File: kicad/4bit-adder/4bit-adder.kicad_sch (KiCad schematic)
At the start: 94 parts, among them J1 Screw_Terminal_01x02, K1 SR11-5V-200-2C-PH, K10 SR11-5V-200-2C-PH, K11 SR11-5V-200-2C-PH, K12 SR11-5V-200-2C-PH, K13 SR11-5V-200-2C-PH, K14 SR11-5V-200-2C-PH, K15 SR11-5V-200-2C-PH, K16 SR11-5V-200-2C-PH, K17 SR11-5V-200-2C-PH, K18 SR11-5V-200-2C-PH, K19 SR11-5V-200-2C-PH, K2 SR11-5V-200-2C-PH, K20 SR11-5V-200-2C-PH, K21 SR11-5V-200-2C-PH, K22 SR11-5V-200-2C-PH, K23 SR11-5V-200-2C-PH, K24 SR11-5V-200-2C-PH, K3 SR11-5V-200-2C-PH, K4 SR11-5V-200-2C-PH, K5 SR11-5V-200-2C-PH, K6 SR11-5V-200-2C-PH, K7 SR11-5V-200-2C-PH, K8 SR11-5V-200-2C-PH, K9 SR11-5V-200-2C-PH, SW1 SW_Wuerth_450301014042, SW3 A, SW4 B

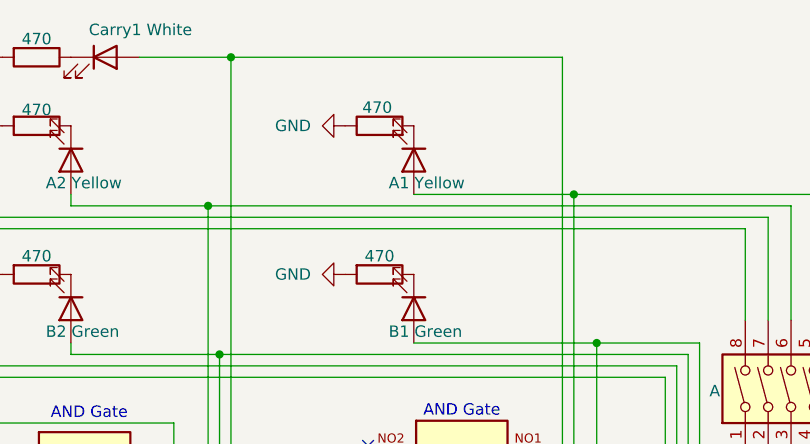
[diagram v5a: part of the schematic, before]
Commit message: wired top pad-A
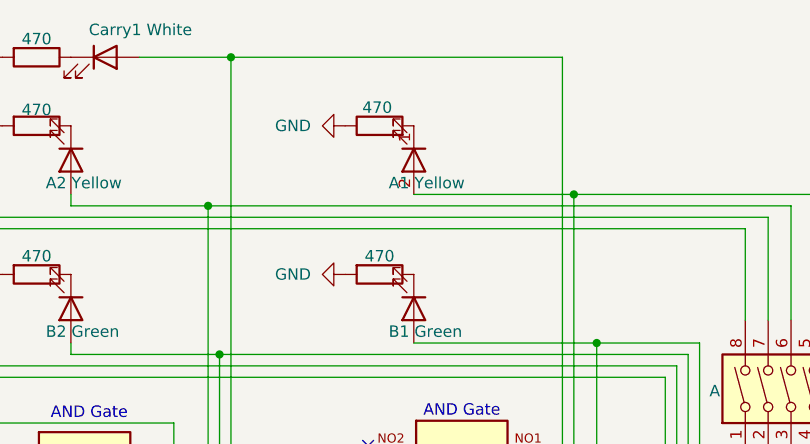
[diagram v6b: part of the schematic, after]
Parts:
- D1, D22, D23, D24, D26, D27, D28, D29, D3, D30, D31, D32, D33, D34, D35, D36, D37, D38, D39, D4, D40, D41, D42, D43, D44, D45, D46, D47, D48, D49, D5, D6, D7: footprint Diode_THT:D_DO-41_SOD81_P10.16mm_Horizontal -> Diode_SMD:D_SOD-123F
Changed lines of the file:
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@@
 			)
 		)
-		(property "Footprint" "Diode_THT:D_DO-41_SOD81_P10.16mm_Horizontal"
+		(property "Footprint" "Diode_SMD:D_SOD-123F"
 			(at 115.57 118.745 0)
 			(hide yes)
@@
 			)
 		)
-		(property "Footprint" "Diode_THT:D_DO-41_SOD81_P10.16mm_Horizontal"
+		(property "Footprint" "Diode_SMD:D_SOD-123F"
 			(at 115.57 95.885 0)
 			(hide yes)
@@
 			)
 		)
-		(property "Footprint" "Diode_THT:D_DO-41_SOD81_P10.16mm_Horizontal"
+		(property "Footprint" "Diode_SMD:D_SOD-123F"
 			(at 36.83 193.675 0)
 			(hide yes)
@@
 			)
 		)
-		(property "Footprint" "Diode_THT:D_DO-41_SOD81_P10.16mm_Horizontal"
+		(property "Footprint" "Diode_SMD:D_SOD-123F"
 			(at 35.56 95.885 0)
 			(hide yes)
@@
 			)
 		)
-		(property "Footprint" "Diode_THT:D_DO-41_SOD81_P10.16mm_Horizontal"
+		(property "Footprint" "Diode_SMD:D_SOD-123F"
 			(at 35.56 168.275 0)
 			(hide yes)
@@
 			)
 		)
-		(property "Footprint" "Diode_THT:D_DO-41_SOD81_P10.16mm_Horizontal"
+		(property "Footprint" "Diode_SMD:D_SOD-123F"
 			(at 99.06 85.725 0)
 			(hide yes)
@@
 			)
 		)
-		(property "Footprint" "Diode_THT:D_DO-41_SOD81_P10.16mm_Horizontal"
+		(property "Footprint" "Diode_SMD:D_SOD-123F"
 			(at 76.2 146.685 0)
 			(hide yes)
@@
 			)
 		)
-		(property "Footprint" "Diode_THT:D_DO-41_SOD81_P10.16mm_Horizontal"
+		(property "Footprint" "Diode_SMD:D_SOD-123F"
 			(at 76.2 118.745 0)
 			(hide yes)
@@
 			)
 		)
-		(property "Footprint" "Diode_THT:D_DO-41_SOD81_P10.16mm_Horizontal"
+		(property "Footprint" "Diode_SMD:D_SOD-123F"
 			(at 35.56 118.745 0)
 			(hide yes)
@@
 			)
 		)
-		(property "Footprint" "Diode_THT:D_DO-41_SOD81_P10.16mm_Horizontal"
+		(property "Footprint" "Diode_SMD:D_SOD-123F"
 			(at 157.48 95.885 0)
 			(hide yes)
@@
 			)
 		)
-		(property "Footprint" "Diode_THT:D_DO-41_SOD81_P10.16mm_Horizontal"
+		(property "Footprint" "Diode_SMD:D_SOD-123F"
 			(at 76.2 168.275 0)
 			(hide yes)
@@
 			)
 		)
-		(property "Footprint" "Diode_THT:D_DO-41_SOD81_P10.16mm_Horizontal"
+		(property "Footprint" "Diode_SMD:D_SOD-123F"
 			(at 76.2 193.675 0)
 			(hide yes)
@@
 			)
 		)
-		(property "Footprint" "Diode_THT:D_DO-41_SOD81_P10.16mm_Horizontal"
+		(property "Footprint" "Diode_SMD:D_SOD-123F"
 			(at 19.05 88.265 0)
 			(hide yes)
@@
 			)
 		)
-		(property "Footprint" "Diode_THT:D_DO-41_SOD81_P10.16mm_Horizontal"
+		(property "Footprint" "Diode_SMD:D_SOD-123F"
 			(at 115.57 146.685 0)
 			(hide yes)
@@
 			)
 		)
-		(property "Footprint" "Diode_THT:D_DO-41_SOD81_P10.16mm_Horizontal"
+		(property "Footprint" "Diode_SMD:D_SOD-123F"
 			(at 115.57 193.675 0)
 			(hide yes)
@@
 			)
 		)
-		(property "Footprint" "Diode_THT:D_DO-41_SOD81_P10.16mm_Horizontal"
+		(property "Footprint" "Diode_SMD:D_SOD-123F"
 			(at 115.57 73.025 0)
 			(hide yes)
@@
 			)
 		)
-		(property "Footprint" "Diode_THT:D_DO-41_SOD81_P10.16mm_Horizontal"
+		(property "Footprint" "Diode_SMD:D_SOD-123F"
 			(at 59.69 83.185 0)
 			(hide yes)
@@
 			)
 		)
-		(property "Footprint" "Diode_THT:D_DO-41_SOD81_P10.16mm_Horizontal"
+		(property "Footprint" "Diode_SMD:D_SOD-123F"
 			(at 19.05 83.185 0)
 			(hide yes)
@@
 			)
 		)
-		(property "Footprint" "Diode_THT:D_DO-41_SOD81_P10.16mm_Horizontal"
+		(property "Footprint" "Diode_SMD:D_SOD-123F"
 			(at 99.06 83.185 0)
 			(hide yes)
@@
 			)
 		)
-		(property "Footprint" "Diode_THT:D_DO-41_SOD81_P10.16mm_Horizontal"
+		(property "Footprint" "Diode_SMD:D_SOD-123F"
 			(at 76.2 215.265 0)
 			(hide yes)
@@
 			)
 		)
-		(property "Footprint" "Diode_THT:D_DO-41_SOD81_P10.16mm_Horizontal"
+		(property "Footprint" "Diode_SMD:D_SOD-123F"
 			(at 35.56 215.265 0)
 			(hide yes)
@@
 	)
 	(symbol
+		(lib_name "LED_1")
 		(lib_id "Device:LED")
 		(at 152.4 29.21 270)
@@
 			)
 		)
-		(property "Footprint" "Diode_THT:D_DO-41_SOD81_P10.16mm_Horizontal"
+		(property "Footprint" "Diode_SMD:D_SOD-123F"
 			(at 157.48 121.285 0)
 			(hide yes)
@@
 			)
 		)
-		(property "Footprint" "Diode_THT:D_DO-41_SOD81_P10.16mm_Horizontal"
+		(property "Footprint" "Diode_SMD:D_SOD-123F"
 			(at 35.56 73.025 0)
 			(hide yes)
@@
 			)
 		)
-		(property "Footprint" "Diode_THT:D_DO-41_SOD81_P10.16mm_Horizontal"
+		(property "Footprint" "Diode_SMD:D_SOD-123F"
 			(at 157.48 71.755 0)
 			(hide yes)
@@
 			)
 		)
-		(property "Footprint" "Diode_THT:D_DO-41_SOD81_P10.16mm_Horizontal"
+		(property "Footprint" "Diode_SMD:D_SOD-123F"
 			(at 35.56 146.685 0)
 			(hide yes)
@@
 			)
 		)
-		(property "Footprint" "Diode_THT:D_DO-41_SOD81_P10.16mm_Horizontal"
+		(property "Footprint" "Diode_SMD:D_SOD-123F"
 			(at 59.69 88.265 0)
 			(hide yes)
@@
 			)
 		)
-		(property "Footprint" "Diode_THT:D_DO-41_SOD81_P10.16mm_Horizontal"
+		(property "Footprint" "Diode_SMD:D_SOD-123F"
 			(at 77.47 95.885 0)
 			(hide yes)
@@
 			)
 		)
-		(property "Footprint" "Diode_THT:D_DO-41_SOD81_P10.16mm_Horizontal"
+		(property "Footprint" "Diode_SMD:D_SOD-123F"
 			(at 115.57 215.265 0)
 			(hide yes)
@@
 			)
 		)
-		(property "Footprint" "Diode_THT:D_DO-41_SOD81_P10.16mm_Horizontal"
+		(property "Footprint" "Diode_SMD:D_SOD-123F"
 			(at 19.05 85.725 0)
 			(hide yes)
@@
 			)
 		)
-		(property "Footprint" "Diode_THT:D_DO-41_SOD81_P10.16mm_Horizontal"
+		(property "Footprint" "Diode_SMD:D_SOD-123F"
 			(at 76.2 73.025 0)
 			(hide yes)
@@
 			)
 		)
-		(property "Footprint" "Diode_THT:D_DO-41_SOD81_P10.16mm_Horizontal"
+		(property "Footprint" "Diode_SMD:D_SOD-123F"
 			(at 99.06 88.265 0)
 			(hide yes)
@@
 			)
 		)
-		(property "Footprint" "Diode_THT:D_DO-41_SOD81_P10.16mm_Horizontal"
+		(property "Footprint" "Diode_SMD:D_SOD-123F"
 			(at 59.69 85.725 0)
 			(hide yes)
@@
 			)
 		)
-		(property "Footprint" "Diode_THT:D_DO-41_SOD81_P10.16mm_Horizontal"
+		(property "Footprint" "Diode_SMD:D_SOD-123F"
 			(at 115.57 168.275 0)
 			(hide yes)

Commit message: finished pcb wiring
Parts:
- D1, D22, D23, D24, D26, D27, D28, D29, D3, D30, D31, D32, D33, D34, D35, D36, D37, D38, D39, D4, D40, D41, D42, D43, D44, D45, D46, D47, D48, D49, D5, D6, D7: footprint Diode_SMD:D_SOD-123F -> Diode_THT:D_T-1_P5.08mm_Horizontal
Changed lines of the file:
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@@
 			)
 		)
-		(property "Footprint" "Diode_SMD:D_SOD-123F"
+		(property "Footprint" "Diode_THT:D_T-1_P5.08mm_Horizontal"
 			(at 115.57 118.745 0)
 			(hide yes)
@@
 	)
 	(symbol
+		(lib_name "1N4003_1")
 		(lib_id "Diode:1N4003")
 		(at 115.57 100.33 180)
@@
 			)
 		)
-		(property "Footprint" "Diode_SMD:D_SOD-123F"
+		(property "Footprint" "Diode_THT:D_T-1_P5.08mm_Horizontal"
 			(at 115.57 95.885 0)
 			(hide yes)
@@
 			)
 		)
-		(property "Footprint" "Diode_SMD:D_SOD-123F"
+		(property "Footprint" "Diode_THT:D_T-1_P5.08mm_Horizontal"
 			(at 36.83 193.675 0)
 			(hide yes)
@@
 			)
 		)
-		(property "Footprint" "Diode_SMD:D_SOD-123F"
+		(property "Footprint" "Diode_THT:D_T-1_P5.08mm_Horizontal"
 			(at 35.56 95.885 0)
 			(hide yes)
@@
 			)
 		)
-		(property "Footprint" "Diode_SMD:D_SOD-123F"
+		(property "Footprint" "Diode_THT:D_T-1_P5.08mm_Horizontal"
 			(at 35.56 168.275 0)
 			(hide yes)
@@
 			)
 		)
-		(property "Footprint" "Diode_SMD:D_SOD-123F"
+		(property "Footprint" "Diode_THT:D_T-1_P5.08mm_Horizontal"
 			(at 99.06 85.725 0)
 			(hide yes)
@@
 			)
 		)
-		(property "Footprint" "Diode_SMD:D_SOD-123F"
+		(property "Footprint" "Diode_THT:D_T-1_P5.08mm_Horizontal"
 			(at 76.2 146.685 0)
 			(hide yes)
@@
 			)
 		)
-		(property "Footprint" "Diode_SMD:D_SOD-123F"
+		(property "Footprint" "Diode_THT:D_T-1_P5.08mm_Horizontal"
 			(at 76.2 118.745 0)
 			(hide yes)
@@
 			)
 		)
-		(property "Footprint" "Diode_SMD:D_SOD-123F"
+		(property "Footprint" "Diode_THT:D_T-1_P5.08mm_Horizontal"
 			(at 35.56 118.745 0)
 			(hide yes)
@@
 			)
 		)
-		(property "Footprint" "Diode_SMD:D_SOD-123F"
+		(property "Footprint" "Diode_THT:D_T-1_P5.08mm_Horizontal"
 			(at 157.48 95.885 0)
 			(hide yes)
@@
 			)
 		)
-		(property "Footprint" "Diode_SMD:D_SOD-123F"
+		(property "Footprint" "Diode_THT:D_T-1_P5.08mm_Horizontal"
 			(at 76.2 168.275 0)
 			(hide yes)
@@
 			)
 		)
-		(property "Footprint" "Diode_SMD:D_SOD-123F"
+		(property "Footprint" "Diode_THT:D_T-1_P5.08mm_Horizontal"
 			(at 76.2 193.675 0)
 			(hide yes)
@@
 			)
 		)
-		(property "Footprint" "Diode_SMD:D_SOD-123F"
+		(property "Footprint" "Diode_THT:D_T-1_P5.08mm_Horizontal"
 			(at 19.05 88.265 0)
 			(hide yes)
@@
 			)
 		)
-		(property "Footprint" "Diode_SMD:D_SOD-123F"
+		(property "Footprint" "Diode_THT:D_T-1_P5.08mm_Horizontal"
 			(at 115.57 146.685 0)
 			(hide yes)
@@
 			)
 		)
-		(property "Footprint" "Diode_SMD:D_SOD-123F"
+		(property "Footprint" "Diode_THT:D_T-1_P5.08mm_Horizontal"
 			(at 115.57 193.675 0)
 			(hide yes)
@@
 			)
 		)
-		(property "Footprint" "Diode_SMD:D_SOD-123F"
+		(property "Footprint" "Diode_THT:D_T-1_P5.08mm_Horizontal"
 			(at 115.57 73.025 0)
 			(hide yes)
@@
 			)
 		)
-		(property "Footprint" "Diode_SMD:D_SOD-123F"
+		(property "Footprint" "Diode_THT:D_T-1_P5.08mm_Horizontal"
 			(at 59.69 83.185 0)
 			(hide yes)
@@
 			)
 		)
-		(property "Footprint" "Diode_SMD:D_SOD-123F"
+		(property "Footprint" "Diode_THT:D_T-1_P5.08mm_Horizontal"
 			(at 19.05 83.185 0)
 			(hide yes)
@@
 			)
 		)
-		(property "Footprint" "Diode_SMD:D_SOD-123F"
+		(property "Footprint" "Diode_THT:D_T-1_P5.08mm_Horizontal"
 			(at 99.06 83.185 0)
 			(hide yes)
@@
 			)
 		)
-		(property "Footprint" "Diode_SMD:D_SOD-123F"
+		(property "Footprint" "Diode_THT:D_T-1_P5.08mm_Horizontal"
 			(at 76.2 215.265 0)
 			(hide yes)
@@
 			)
 		)
-		(property "Footprint" "Diode_SMD:D_SOD-123F"
+		(property "Footprint" "Diode_THT:D_T-1_P5.08mm_Horizontal"
 			(at 35.56 215.265 0)
 			(hide yes)
@@
 			)
 		)
-		(property "Footprint" "Diode_SMD:D_SOD-123F"
+		(property "Footprint" "Diode_THT:D_T-1_P5.08mm_Horizontal"
 			(at 157.48 121.285 0)
 			(hide yes)
@@
 			)
 		)
-		(property "Footprint" "Diode_SMD:D_SOD-123F"
+		(property "Footprint" "Diode_THT:D_T-1_P5.08mm_Horizontal"
 			(at 35.56 73.025 0)
 			(hide yes)
@@
 			)
 		)
-		(property "Footprint" "Diode_SMD:D_SOD-123F"
+		(property "Footprint" "Diode_THT:D_T-1_P5.08mm_Horizontal"
 			(at 157.48 71.755 0)
 			(hide yes)
@@
 			)
 		)
-		(property "Footprint" "Diode_SMD:D_SOD-123F"
+		(property "Footprint" "Diode_THT:D_T-1_P5.08mm_Horizontal"
 			(at 35.56 146.685 0)
 			(hide yes)
@@
 			)
 		)
-		(property "Footprint" "Diode_SMD:D_SOD-123F"
+		(property "Footprint" "Diode_THT:D_T-1_P5.08mm_Horizontal"
 			(at 59.69 88.265 0)
 			(hide yes)
@@
 			)
 		)
-		(property "Footprint" "Diode_SMD:D_SOD-123F"
+		(property "Footprint" "Diode_THT:D_T-1_P5.08mm_Horizontal"
 			(at 77.47 95.885 0)
 			(hide yes)
@@
 			)
 		)
-		(property "Footprint" "Diode_SMD:D_SOD-123F"
+		(property "Footprint" "Diode_THT:D_T-1_P5.08mm_Horizontal"
 			(at 115.57 215.265 0)
 			(hide yes)
@@
 			)
 		)
-		(property "Footprint" "Diode_SMD:D_SOD-123F"
+		(property "Footprint" "Diode_THT:D_T-1_P5.08mm_Horizontal"
 			(at 19.05 85.725 0)
 			(hide yes)
@@
 			)
 		)
-		(property "Footprint" "Diode_SMD:D_SOD-123F"
+		(property "Footprint" "Diode_THT:D_T-1_P5.08mm_Horizontal"
 			(at 76.2 73.025 0)
 			(hide yes)
@@
 			)
 		)
-		(property "Footprint" "Diode_SMD:D_SOD-123F"
+		(property "Footprint" "Diode_THT:D_T-1_P5.08mm_Horizontal"
 			(at 99.06 88.265 0)
 			(hide yes)
@@
 			)
 		)
-		(property "Footprint" "Diode_SMD:D_SOD-123F"
+		(property "Footprint" "Diode_THT:D_T-1_P5.08mm_Horizontal"
 			(at 59.69 85.725 0)
 			(hide yes)
@@
 			)
 		)
-		(property "Footprint" "Diode_SMD:D_SOD-123F"
+		(property "Footprint" "Diode_THT:D_T-1_P5.08mm_Horizontal"
 			(at 115.57 168.275 0)
 			(hide yes)
